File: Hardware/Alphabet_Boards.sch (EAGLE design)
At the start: 59 parts

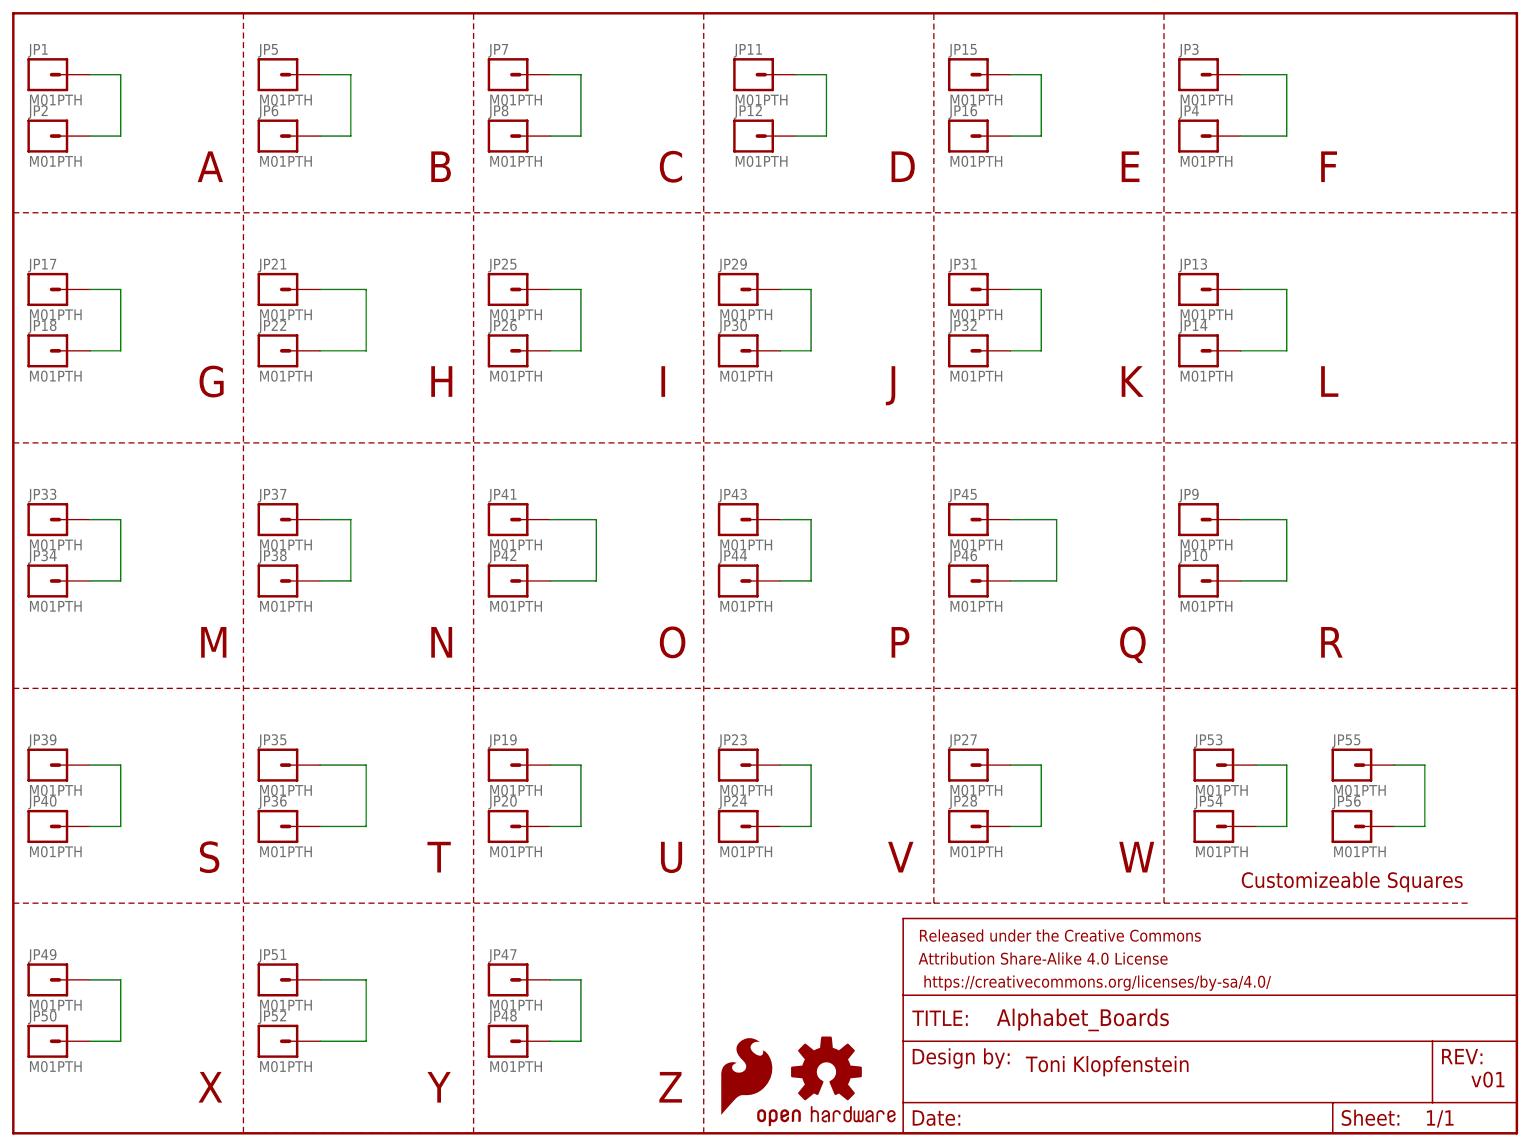
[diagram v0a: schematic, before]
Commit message: Updating letter boards to be blank
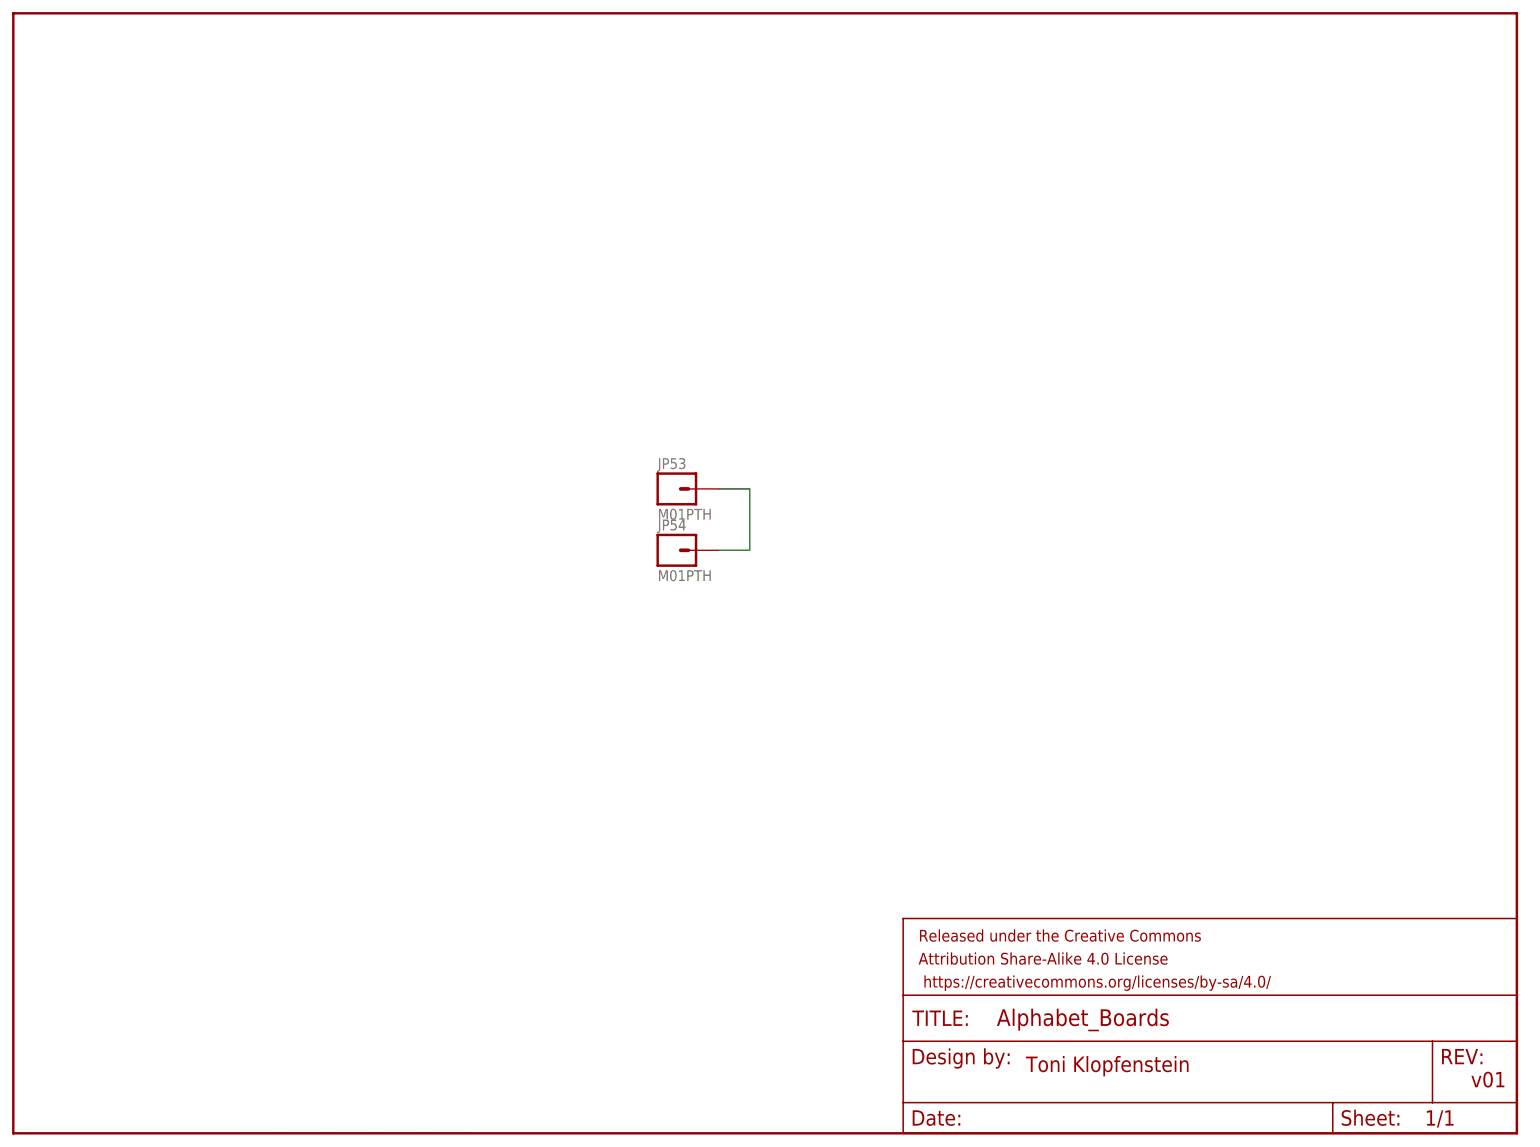
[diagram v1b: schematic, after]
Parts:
- removed JP1, JP10, JP11, JP12, JP13, JP14, JP15, JP16, JP17, JP18, JP19, JP2, JP20, JP21, JP22, JP23, JP24, JP25, JP26, JP27, JP28, JP29, JP3, JP30, JP31, JP32, JP33, JP34, JP35, JP36, JP37, JP38, JP39, JP4, JP40, JP41, JP42, JP43, JP44, JP45, JP46, JP47, JP48, JP49, JP5, JP50, JP51, JP52, JP55, JP56, JP6, JP7, JP8, JP9: M01PTH, SparkFun-Connectors:M01PTH
- removed LOGO29: OSHW-LOGOS, SparkFun-Aesthetics:OSHW-LOGOS
- removed LOGO56: SFE_LOGO_FLAME.1_INCH, SparkFun-Aesthetics:SFE_LOGO_FLAME.1_INCH
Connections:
- removed net N$1: JP1.1, JP2.1
- removed net N$10: JP31.1, JP32.1
- removed net N$11: JP13.1, JP14.1
- removed net N$12: JP37.1, JP38.1
- removed net N$13: JP41.1, JP42.1
- removed net N$14: JP43.1, JP44.1
- removed net N$15: JP45.1, JP46.1
- removed net N$16: JP10.1, JP9.1
- removed net N$17: JP35.1, JP36.1
- removed net N$18: JP19.1, JP20.1
- removed net N$19: JP23.1, JP24.1
- removed net N$2: JP5.1, JP6.1
- removed net N$20: JP27.1, JP28.1
- removed net N$21: JP51.1, JP52.1
- removed net N$22: JP47.1, JP48.1
- removed net N$23: JP17.1, JP18.1
- removed net N$24: JP33.1, JP34.1
- removed net N$25: JP39.1, JP40.1
- removed net N$26: JP49.1, JP50.1
- removed net N$28: JP55.1, JP56.1
- removed net N$3: JP7.1, JP8.1
- removed net N$4: JP11.1, JP12.1
- removed net N$5: JP15.1, JP16.1
- removed net N$6: JP3.1, JP4.1
- removed net N$7: JP21.1, JP22.1
- removed net N$8: JP25.1, JP26.1
- removed net N$9: JP29.1, JP30.1
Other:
- note removed: "A"
- note removed: "B"
- note removed: "C"
- note removed: "Customizeable Squares"
- note removed: "D"
- note removed: "E"
- note removed: "F"
- note removed: "G"
- note removed: "H"
- note removed: "I"
- note removed: "J"
- note removed: "K"
- note removed: "L"
- note removed: "M"
- note removed: "N"
- note removed: "O"
- note removed: "P"
- note removed: "Q"
- note removed: "R"
- note removed: "S"
- note removed: "T"
- note removed: "U"
- note removed: "V"
- note removed: "W"
- note removed: "X"
- note removed: "Y"
- note removed: "Z"
- moved on the sheet: JP53, JP54

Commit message: Updating to Scrabble distribution
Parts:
- removed JP53, JP54: M01PTH, SparkFun-Connectors:M01PTH
- added U$1, U$10, U$100, U$11, U$12, U$13, U$14, U$15, U$16, U$17, U$18, U$19, U$2, U$20, U$21, U$22, U$23, U$24, U$25, U$26, U$27, U$28, U$29, U$3, U$30, U$31, U$32, U$33, U$34, U$35, U$36, U$37, U$38, U$39, U$4, U$40, U$41, U$42, U$43, U$44, U$45, U$46, U$47, U$48, U$49, U$5, U$50, U$51, U$52, U$53, U$54, U$55, U$56, U$57, U$58, U$59, U$6, U$60, U$61, U$62, U$63, U$64, U$65, U$66, U$67, U$68, U$69, U$7, U$70, U$71, U$72, U$73, U$74, U$75, U$76, U$77, U$78, U$79, U$8, U$80, U$81, U$82, U$83, U$84, U$85, U$86, U$87, U$88, U$89, U$9, U$90, U$91, U$92, U$93, U$94, U$95, U$96, U$97, U$98, U$99: ALPHABET, Local Library:ALPHABET
- FRAME1: value FRAME-LETTER -> FRAME-LEDGER; device SparkFun-Aesthetics:FRAME-LETTER -> SparkFun-Aesthetics:FRAME-LEDGER
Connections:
- removed net N$27: JP53.1, JP54.1
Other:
- note added: "Based on Scrabble Letter Distribution for English: https://en.wikipedia.org/wiki/Scrabble_letter_distributions#English"
